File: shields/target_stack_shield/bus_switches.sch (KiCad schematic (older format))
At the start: 4 parts

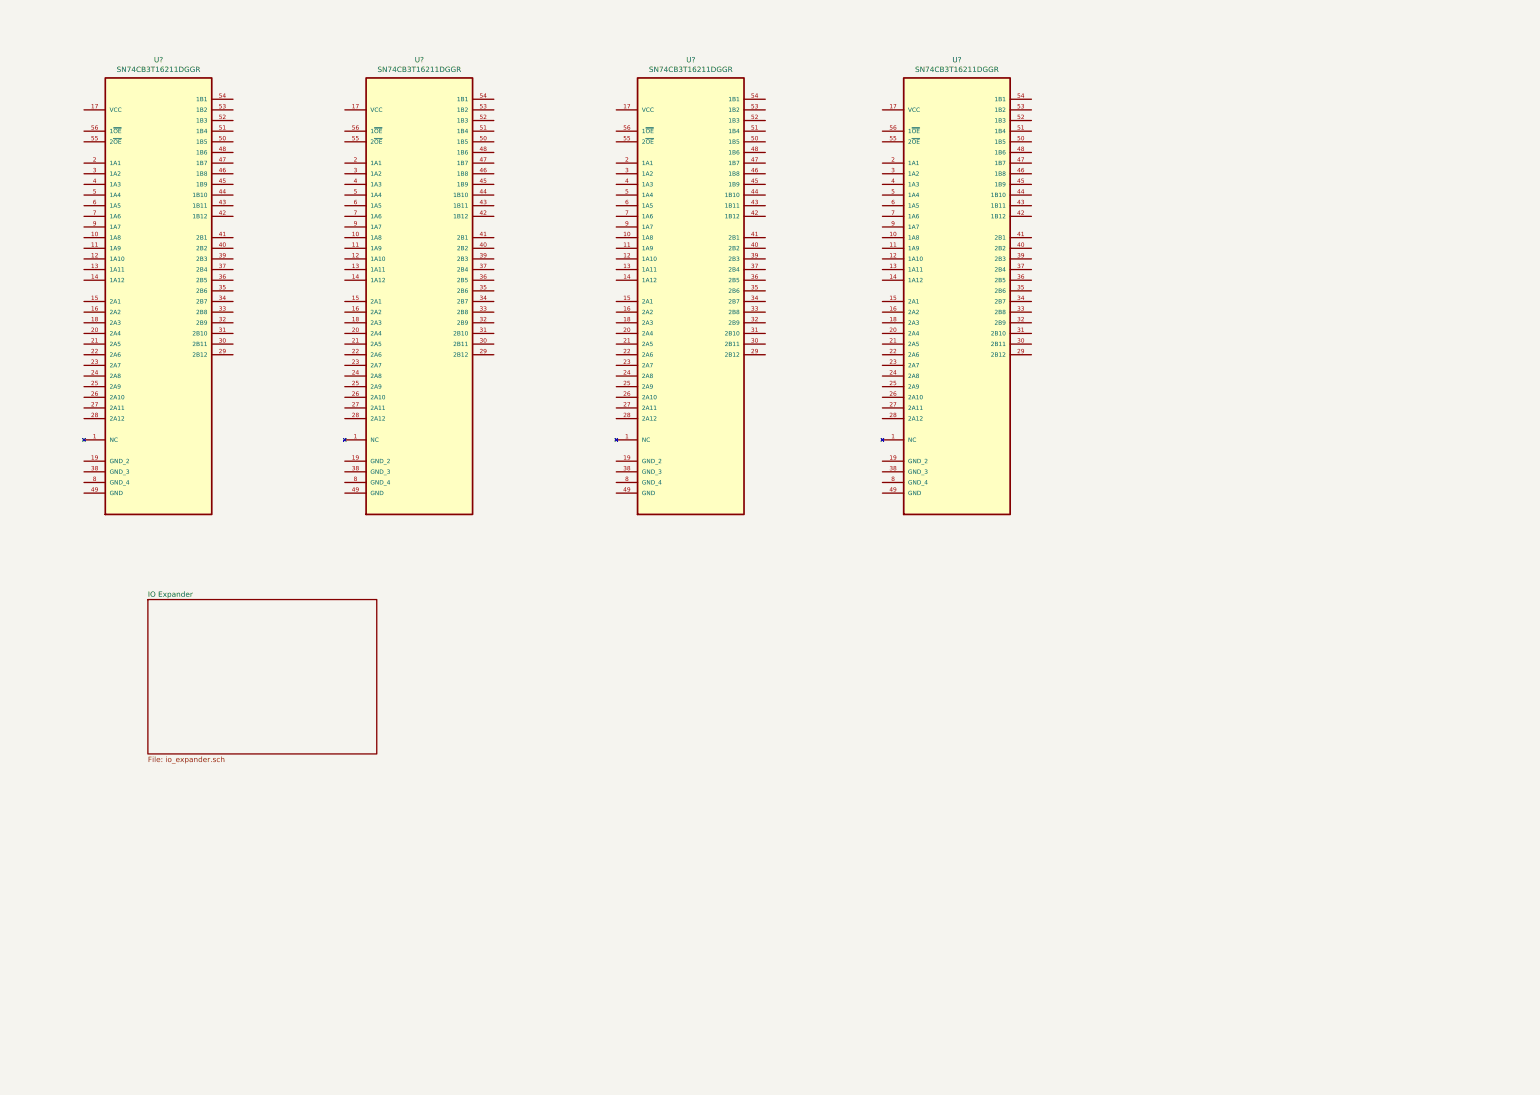
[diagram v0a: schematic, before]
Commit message: further work on target stack shield schematics
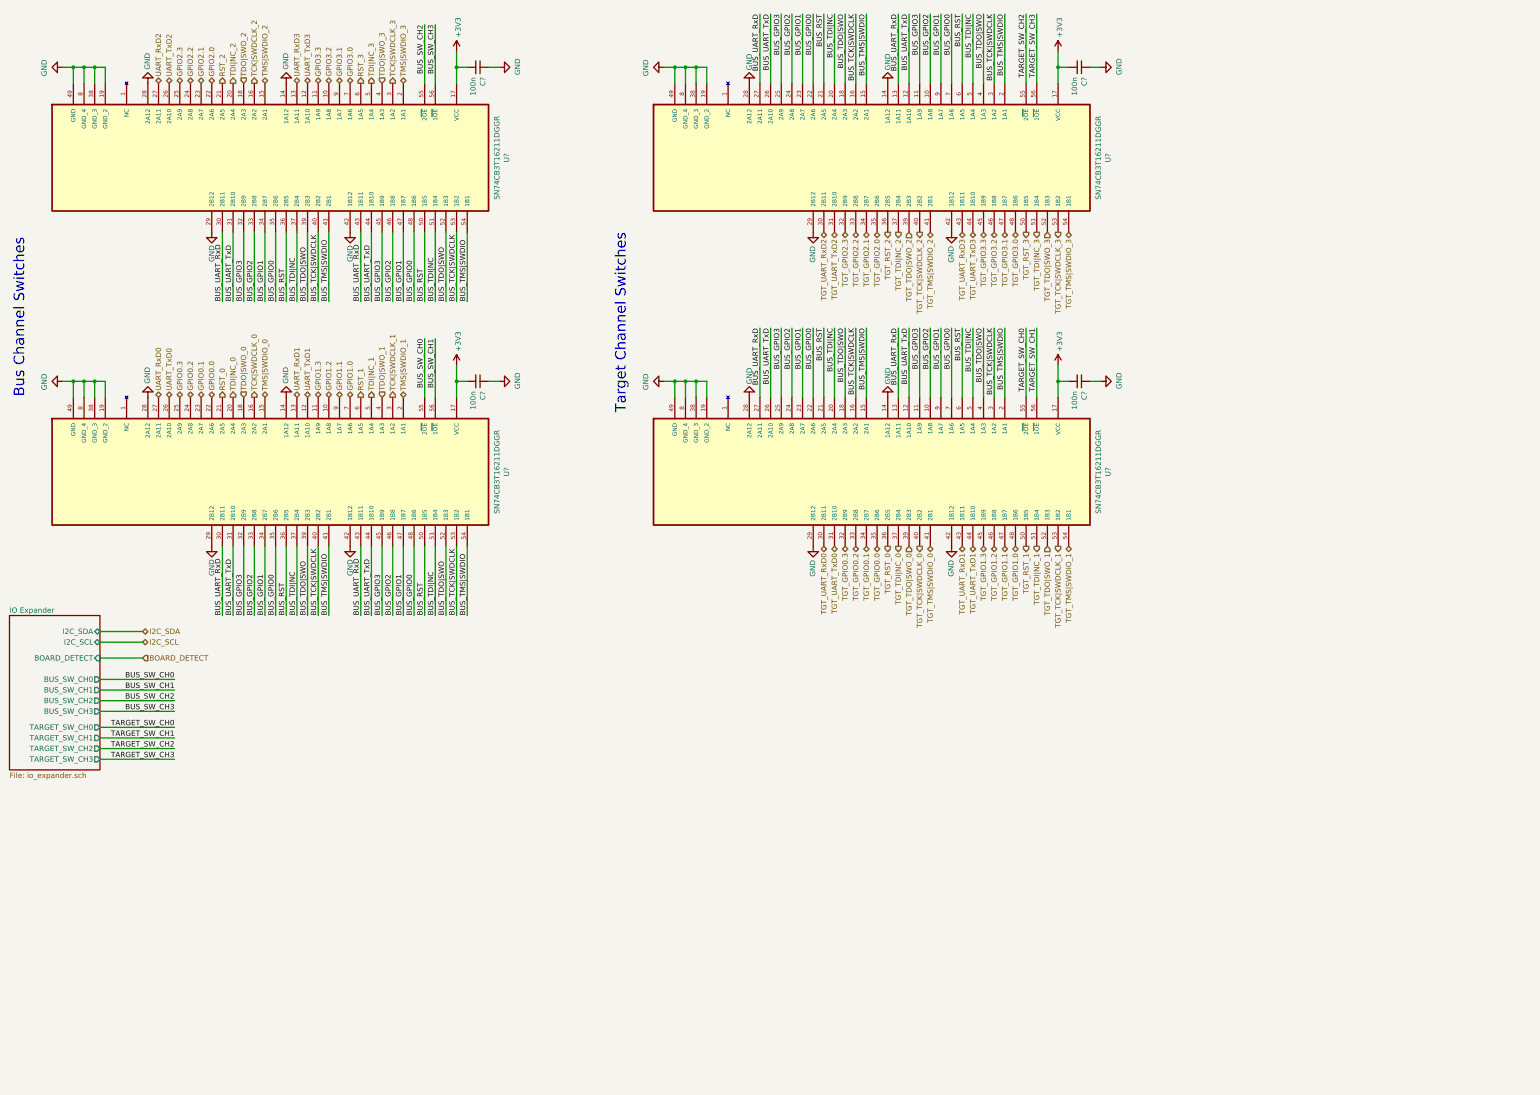
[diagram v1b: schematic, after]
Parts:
- added C? (x4): 100n, symbol Device:C_Small
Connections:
- net GPIO1.2: now reaches U?.10 (1A8)
- net GPIO1.3: now reaches U?.11 (1A9)
- net UART_TxD1: now reaches U?.12 (1A10)
- net UART_RxD1: now reaches U?.13 (1A11)
- net GND: now reaches U?.14 (1A12)
- net GND: now also U?.14 (1A12), U?.14 (1A12), U?.14 (1A12), U?.19 (GND_2), U?.19 (GND_2), U?.19 (GND_2), U?.19 (GND_2), U?.28 (2A12), U?.28 (2A12), U?.28 (2A12), U?.28 (2A12), U?.29 (2B12), U?.29 (2B12), U?.29 (2B12), U?.29 (2B12), U?.38 (GND_3), U?.38 (GND_3), U?.38 (GND_3), U?.38 (GND_3), U?.42 (1B12), U?.42 (1B12), U?.42 (1B12), U?.42 (1B12), U?.49 (GND), U?.49 (GND), U?.49 (GND), U?.49 (GND), U?.8 (GND_4), U?.8 (GND_4), U?.8 (GND_4), U?.8 (GND_4), C?.1, C?.1, C?.1, C?.1
- net TMS|SWDIO_0: now reaches U?.15 (2A1)
- net TCK|SWDCLK_0: now reaches U?.16 (2A2)
- net +3V3: now reaches U?.17 (VCC)
- net +3V3: now also U?.17 (VCC), U?.17 (VCC), U?.17 (VCC), C?.2, C?.2, C?.2, C?.2
- net TDO|SWO_0: now reaches U?.18 (2A3)
- net TMS|SWDIO_1: now reaches U?.2 (1A1)
- net TDI|NC_0: now reaches U?.20 (2A4)
- net RST_0: now reaches U?.21 (2A5)
- net GPIO0.0: now reaches U?.22 (2A6)
- net GPIO0.1: now reaches U?.23 (2A7)
- net GPIO0.2: now reaches U?.24 (2A8)
- net GPIO0.3: now reaches U?.25 (2A9)
- net UART_TxD0: now reaches U?.26 (2A10)
- net UART_RxD0: now reaches U?.27 (2A11)
- net TCK|SWDCLK_1: now reaches U?.3 (1A2)
- net BUS_UART_RxD: now reaches U?.30 (2B11)
- net BUS_UART_RxD: now also U?.13 (1A11), U?.13 (1A11), U?.27 (2A11), U?.27 (2A11), U?.30 (2B11), U?.43 (1B11), U?.43 (1B11)
- net BUS_UART_TxD: now reaches U?.31 (2B10)
- net BUS_UART_TxD: now also U?.12 (1A10), U?.12 (1A10), U?.26 (2A10), U?.26 (2A10), U?.31 (2B10), U?.44 (1B10), U?.44 (1B10)
- net BUS_GPIO3: now reaches U?.32 (2B9)
- net BUS_GPIO3: now also U?.11 (1A9), U?.11 (1A9), U?.25 (2A9), U?.25 (2A9), U?.32 (2B9), U?.45 (1B9), U?.45 (1B9)
- net BUS_GPIO2: now reaches U?.33 (2B8)
- net BUS_GPIO2: now also U?.10 (1A8), U?.10 (1A8), U?.24 (2A8), U?.24 (2A8), U?.33 (2B8), U?.46 (1B8), U?.46 (1B8)
- net BUS_GPIO1: now reaches U?.34 (2B7)
- net BUS_GPIO1: now also U?.23 (2A7), U?.23 (2A7), U?.34 (2B7), U?.47 (1B7), U?.47 (1B7), U?.9 (1A7), U?.9 (1A7)
- net BUS_GPIO0: now reaches U?.35 (2B6)
- net BUS_GPIO0: now also U?.22 (2A6), U?.22 (2A6), U?.35 (2B6), U?.48 (1B6), U?.48 (1B6), U?.7 (1A6), U?.7 (1A6)
- net BUS_RST: now reaches U?.36 (2B5)
- net BUS_RST: now also U?.21 (2A5), U?.21 (2A5), U?.36 (2B5), U?.50 (1B5), U?.50 (1B5), U?.6 (1A5), U?.6 (1A5)
- net BUS_TDI|NC: now reaches U?.37 (2B4)
- net BUS_TDI|NC: now also U?.20 (2A4), U?.20 (2A4), U?.37 (2B4), U?.5 (1A4), U?.5 (1A4), U?.51 (1B4), U?.51 (1B4)
- net BUS_TDO|SWO: now reaches U?.39 (2B3)
- net BUS_TDO|SWO: now also U?.18 (2A3), U?.18 (2A3), U?.39 (2B3), U?.4 (1A3), U?.4 (1A3), U?.52 (1B3), U?.52 (1B3)
- net TDO|SWO_1: now reaches U?.4 (1A3)
- net BUS_TCK|SWDCLK: now reaches U?.40 (2B2)
- net BUS_TCK|SWDCLK: now also U?.16 (2A2), U?.16 (2A2), U?.3 (1A2), U?.3 (1A2), U?.40 (2B2), U?.53 (1B2), U?.53 (1B2)
- net BUS_TMS|SWDIO: now reaches U?.41 (2B1)
- net BUS_TMS|SWDIO: now also U?.15 (2A1), U?.15 (2A1), U?.2 (1A1), U?.2 (1A1), U?.41 (2B1), U?.54 (1B1), U?.54 (1B1)
- net TDI|NC_1: now reaches U?.5 (1A4)
- net BUS_SW_CH0: now reaches U?.55 (2~OE)
- net BUS_SW_CH1: now reaches U?.56 (1~OE)
- net RST_1: now reaches U?.6 (1A5)
- net GPIO1.0: now reaches U?.7 (1A6)
- net GPIO1.1: now reaches U?.9 (1A7)
- net GPIO3.2: now reaches U?.10 (1A8)
- net GPIO3.3: now reaches U?.11 (1A9)
- net UART_TxD3: now reaches U?.12 (1A10)
- net UART_RxD3: now reaches U?.13 (1A11)
- net TMS|SWDIO_2: now reaches U?.15 (2A1)
- net TCK|SWDCLK_2: now reaches U?.16 (2A2)
- net TDO|SWO_2: now reaches U?.18 (2A3)
- net TMS|SWDIO_3: now reaches U?.2 (1A1)
- net TDI|NC_2: now reaches U?.20 (2A4)
- net RST_2: now reaches U?.21 (2A5)
- net GPIO2.0: now reaches U?.22 (2A6)
- net GPIO2.1: now reaches U?.23 (2A7)
- net GPIO2.2: now reaches U?.24 (2A8)
- net GPIO2.3: now reaches U?.25 (2A9)
- net UART_TxD2: now reaches U?.26 (2A10)
- net UART_RxD2: now reaches U?.27 (2A11)
- net TCK|SWDCLK_3: now reaches U?.3 (1A2)
- net TDO|SWO_3: now reaches U?.4 (1A3)
- net TDI|NC_3: now reaches U?.5 (1A4)
- net BUS_SW_CH2: now reaches U?.55 (2~OE)
- net BUS_SW_CH3: now reaches U?.56 (1~OE)
- net RST_3: now reaches U?.6 (1A5)
- net GPIO3.0: now reaches U?.7 (1A6)
- net GPIO3.1: now reaches U?.9 (1A7)
- net TGT_UART_RxD2: now reaches U?.30 (2B11)
- net TGT_UART_TxD2: now reaches U?.31 (2B10)
- net TGT_GPIO2.3: now reaches U?.32 (2B9)
- net TGT_GPIO2.2: now reaches U?.33 (2B8)
- net TGT_GPIO2.1: now reaches U?.34 (2B7)
- net TGT_GPIO2.0: now reaches U?.35 (2B6)
- net TGT_RST_2: now reaches U?.36 (2B5)
- net TGT_TDI|NC_2: now reaches U?.37 (2B4)
- net TGT_TDO|SWO_2: now reaches U?.39 (2B3)
- net TGT_TCK|SWDCLK_2: now reaches U?.40 (2B2)
- net TGT_TMS|SWDIO_2: now reaches U?.41 (2B1)
- net TGT_UART_RxD3: now reaches U?.43 (1B11)
- net TGT_UART_TxD3: now reaches U?.44 (1B10)
- net TGT_GPIO3.3: now reaches U?.45 (1B9)
- net TGT_GPIO3.2: now reaches U?.46 (1B8)
- net TGT_GPIO3.1: now reaches U?.47 (1B7)
- net TGT_GPIO3.0: now reaches U?.48 (1B6)
- net TGT_RST_3: now reaches U?.50 (1B5)
- net TGT_TDI|NC_3: now reaches U?.51 (1B4)
- net TGT_TDO|SWO_3: now reaches U?.52 (1B3)
- net TGT_TCK|SWDCLK_3: now reaches U?.53 (1B2)
- net TGT_TMS|SWDIO_3: now reaches U?.54 (1B1)
- net TARGET_SW_CH2: now reaches U?.55 (2~OE)
- net TARGET_SW_CH3: now reaches U?.56 (1~OE)
- net TGT_UART_RxD0: now reaches U?.30 (2B11)
- net TGT_UART_TxD0: now reaches U?.31 (2B10)
- net TGT_GPIO0.3: now reaches U?.32 (2B9)
- net TGT_GPIO0.2: now reaches U?.33 (2B8)
- net TGT_GPIO0.1: now reaches U?.34 (2B7)
- net TGT_GPIO0.0: now reaches U?.35 (2B6)
- net TGT_RST_0: now reaches U?.36 (2B5)
- net TGT_TDI|NC_0: now reaches U?.37 (2B4)
- net TGT_TDO|SWO_0: now reaches U?.39 (2B3)
- net TGT_TCK|SWDCLK_0: now reaches U?.40 (2B2)
- net TGT_TMS|SWDIO_0: now reaches U?.41 (2B1)
- net TGT_UART_RxD1: now reaches U?.43 (1B11)
- net TGT_UART_TxD1: now reaches U?.44 (1B10)
- net TGT_GPIO1.3: now reaches U?.45 (1B9)
- net TGT_GPIO1.2: now reaches U?.46 (1B8)
- net TGT_GPIO1.1: now reaches U?.47 (1B7)
- net TGT_GPIO1.0: now reaches U?.48 (1B6)
- net TGT_RST_1: now reaches U?.50 (1B5)
- net TGT_TDI|NC_1: now reaches U?.51 (1B4)
- net TGT_TDO|SWO_1: now reaches U?.52 (1B3)
- net TGT_TCK|SWDCLK_1: now reaches U?.53 (1B2)
- net TGT_TMS|SWDIO_1: now reaches U?.54 (1B1)
- net TARGET_SW_CH0: now reaches U?.55 (2~OE)
- net TARGET_SW_CH1: now reaches U?.56 (1~OE)
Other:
- note added: "Bus Channel Switches"
- note added: "Target Channel Switches"
- moved on the sheet: U?

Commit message: implemented changes according to feedback, finished target shield schematics
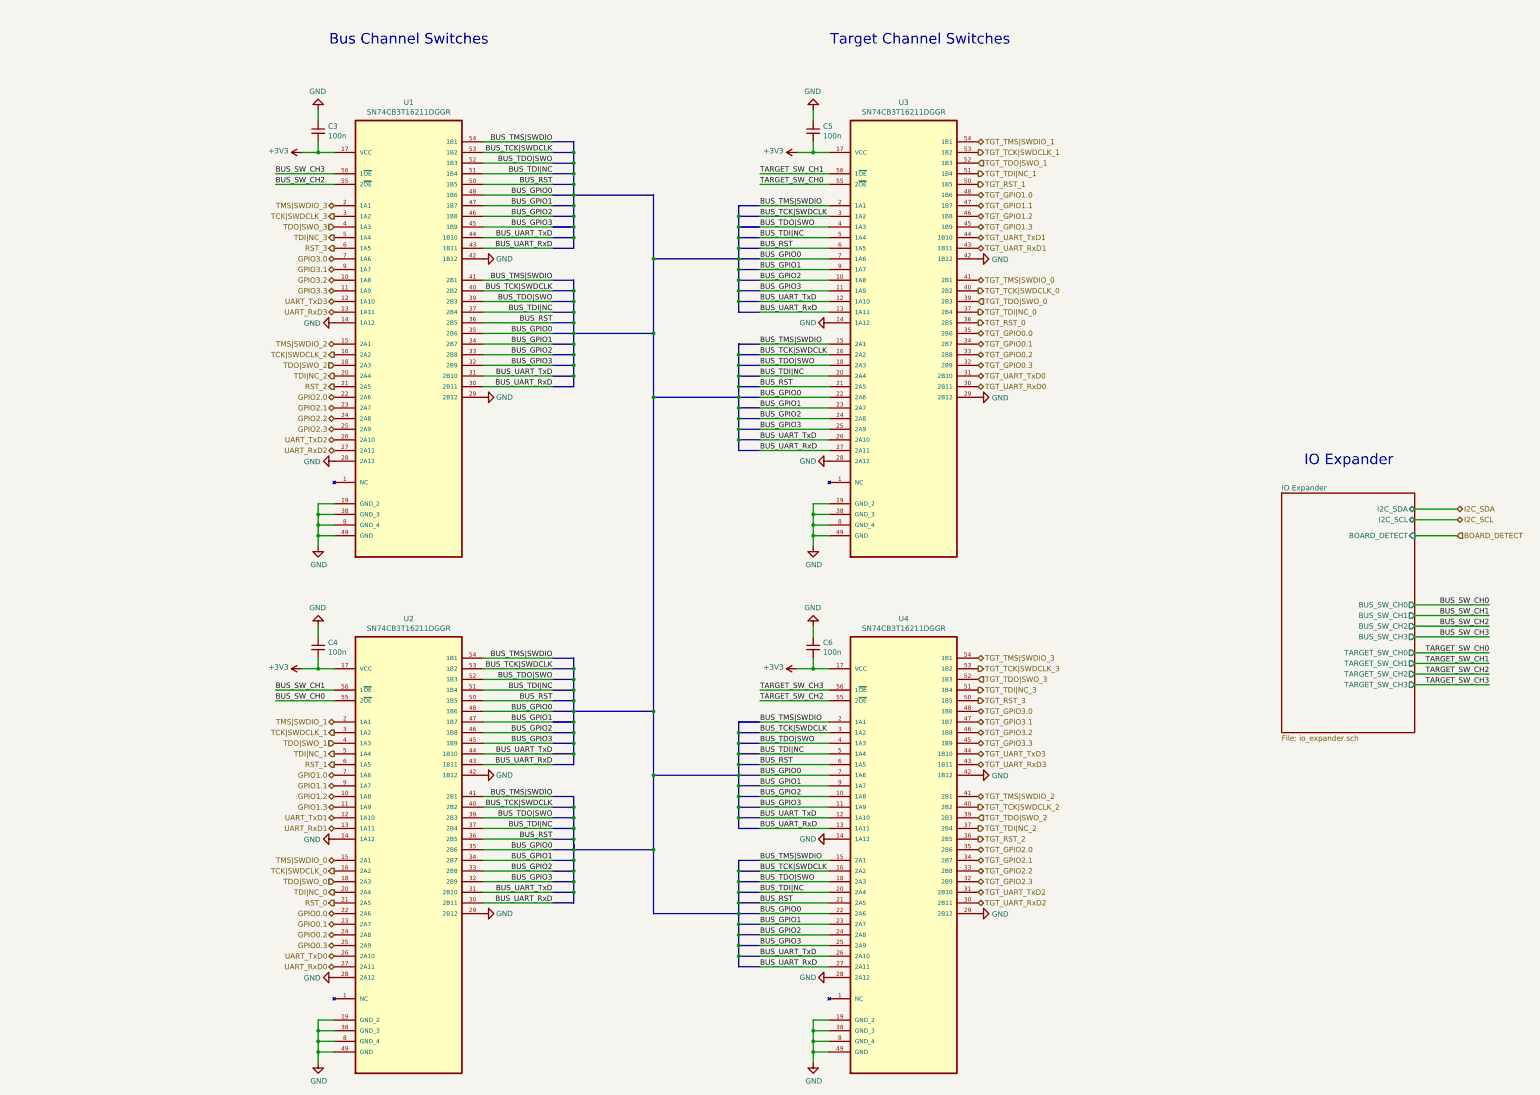
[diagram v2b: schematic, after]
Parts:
- gave numbers to parts that had none: 8
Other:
- note added: "IO Expander"
- moved on the sheet: C3, C4, C5, C6, U1, U2, U3, U4

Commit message: work on target stack shield layout
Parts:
- C3, C4, C5, C6: footprint (none) -> Capacitor_SMD:C_0603_1608Metric_Pad1.05x0.95mm_HandSolder
- U1, U2, U3, U4: footprint SOP50P810X120-56N -> hive:SOP50P810X120-56N
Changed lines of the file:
@@
 F 0 "U2" H 4400 10420 50  0000 C CNN
 F 1 "SN74CB3T16211DGGR" H 4400 10329 50  0000 C CNN
-F 2 "SOP50P810X120-56N" H 4400 8350 50  0001 L BNN
+F 2 "hive:SOP50P810X120-56N" H 4400 8350 50  0001 L BNN
 F 3 "" H 4400 8350 50  0001 L BNN
 F 4 "90H3648" H 4400 8350 50  0001 L BNN "OC_NEWARK"
@@
 F 0 "C4" H 3642 6596 50  0000 L CNN
 F 1 "100n" H 3642 6505 50  0000 L CNN
-F 2 "" H 3550 6550 50  0001 C CNN
+F 2 "Capacitor_SMD:C_0603_1608Metric_Pad1.05x0.95mm_HandSolder" H 3550 6550 50  0001 C CNN
 F 3 "~" H 3550 6550 50  0001 C CNN
 	1    3550 6550
@@
 F 0 "C6" H 8292 6596 50  0000 L CNN
 F 1 "100n" H 8292 6505 50  0000 L CNN
-F 2 "" H 8200 6550 50  0001 C CNN
+F 2 "Capacitor_SMD:C_0603_1608Metric_Pad1.05x0.95mm_HandSolder" H 8200 6550 50  0001 C CNN
 F 3 "~" H 8200 6550 50  0001 C CNN
 	1    8200 6550
@@
 F 0 "C5" H 8292 1746 50  0000 L CNN
 F 1 "100n" H 8292 1655 50  0000 L CNN
-F 2 "" H 8200 1700 50  0001 C CNN
+F 2 "Capacitor_SMD:C_0603_1608Metric_Pad1.05x0.95mm_HandSolder" H 8200 1700 50  0001 C CNN
 F 3 "~" H 8200 1700 50  0001 C CNN
 	1    8200 1700
@@
 F 0 "C3" H 3642 1746 50  0000 L CNN
 F 1 "100n" H 3642 1655 50  0000 L CNN
-F 2 "" H 3550 1700 50  0001 C CNN
+F 2 "Capacitor_SMD:C_0603_1608Metric_Pad1.05x0.95mm_HandSolder" H 3550 1700 50  0001 C CNN
 F 3 "~" H 3550 1700 50  0001 C CNN
 	1    3550 1700
@@
 F 0 "U1" H 4400 5570 50  0000 C CNN
 F 1 "SN74CB3T16211DGGR" H 4400 5479 50  0000 C CNN
-F 2 "SOP50P810X120-56N" H 4400 3500 50  0001 L BNN
+F 2 "hive:SOP50P810X120-56N" H 4400 3500 50  0001 L BNN
 F 3 "" H 4400 3500 50  0001 L BNN
 F 4 "90H3648" H 4400 3500 50  0001 L BNN "OC_NEWARK"
@@
 F 0 "U3" H 9050 5570 50  0000 C CNN
 F 1 "SN74CB3T16211DGGR" H 9050 5479 50  0000 C CNN
-F 2 "SOP50P810X120-56N" H 9050 3500 50  0001 L BNN
+F 2 "hive:SOP50P810X120-56N" H 9050 3500 50  0001 L BNN
 F 3 "" H 9050 3500 50  0001 L BNN
 F 4 "90H3648" H 9050 3500 50  0001 L BNN "OC_NEWARK"
@@
 F 0 "U4" H 9050 10420 50  0000 C CNN
 F 1 "SN74CB3T16211DGGR" H 9050 10329 50  0000 C CNN
-F 2 "SOP50P810X120-56N" H 9050 8350 50  0001 L BNN
+F 2 "hive:SOP50P810X120-56N" H 9050 8350 50  0001 L BNN
 F 3 "" H 9050 8350 50  0001 L BNN
 F 4 "90H3648" H 9050 8350 50  0001 L BNN "OC_NEWARK"
